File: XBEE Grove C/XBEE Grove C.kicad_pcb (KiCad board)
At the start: 2 copper layers, 53.7 x 72.6 mm, 47 parts, among them J12 TSW-102-07-G-S, J13 TSW-103-07-G-S, J2 B2B-PH-K-S, Q1 SI2323DS-T1-E3, U1 FT232RL-REEL, U2 RT9167A-33GB

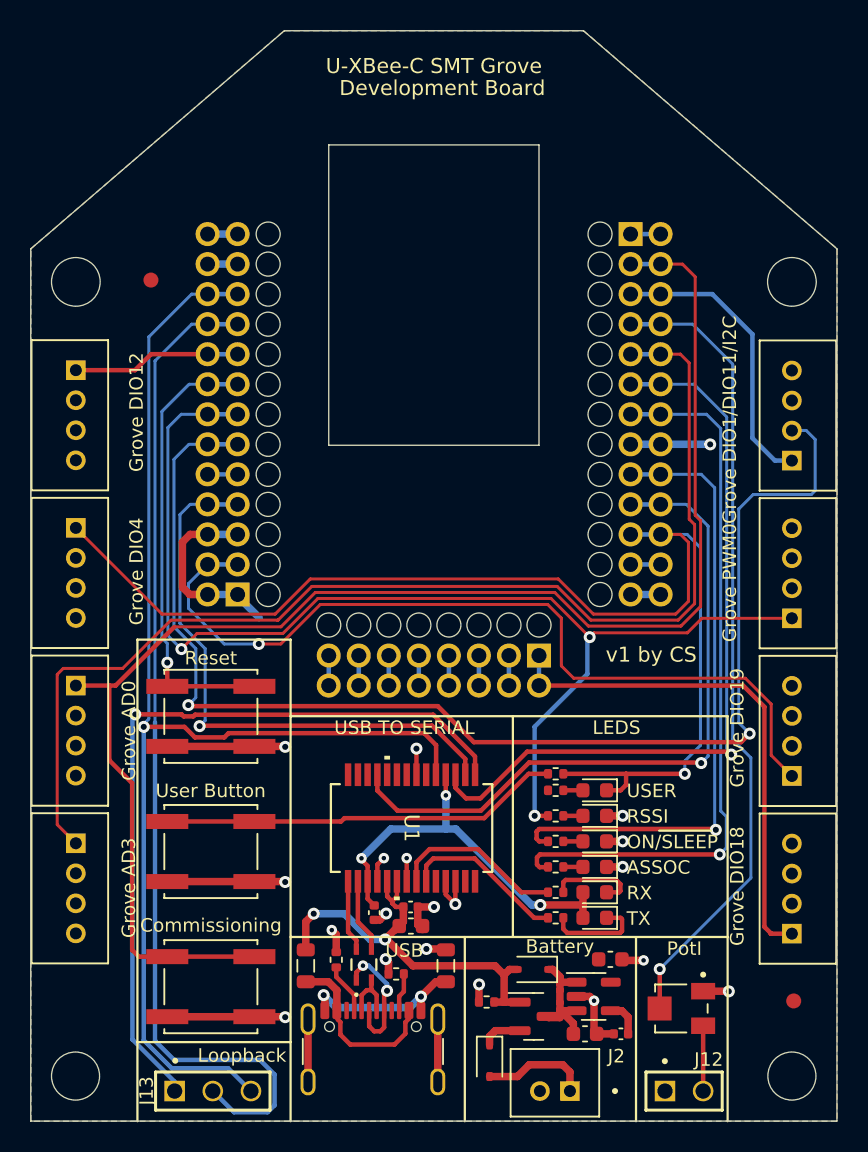
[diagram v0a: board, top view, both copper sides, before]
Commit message: Add files via upload
Corrected L1 and L2 footprints and uploaded boardview file for use with OpenBoardView.
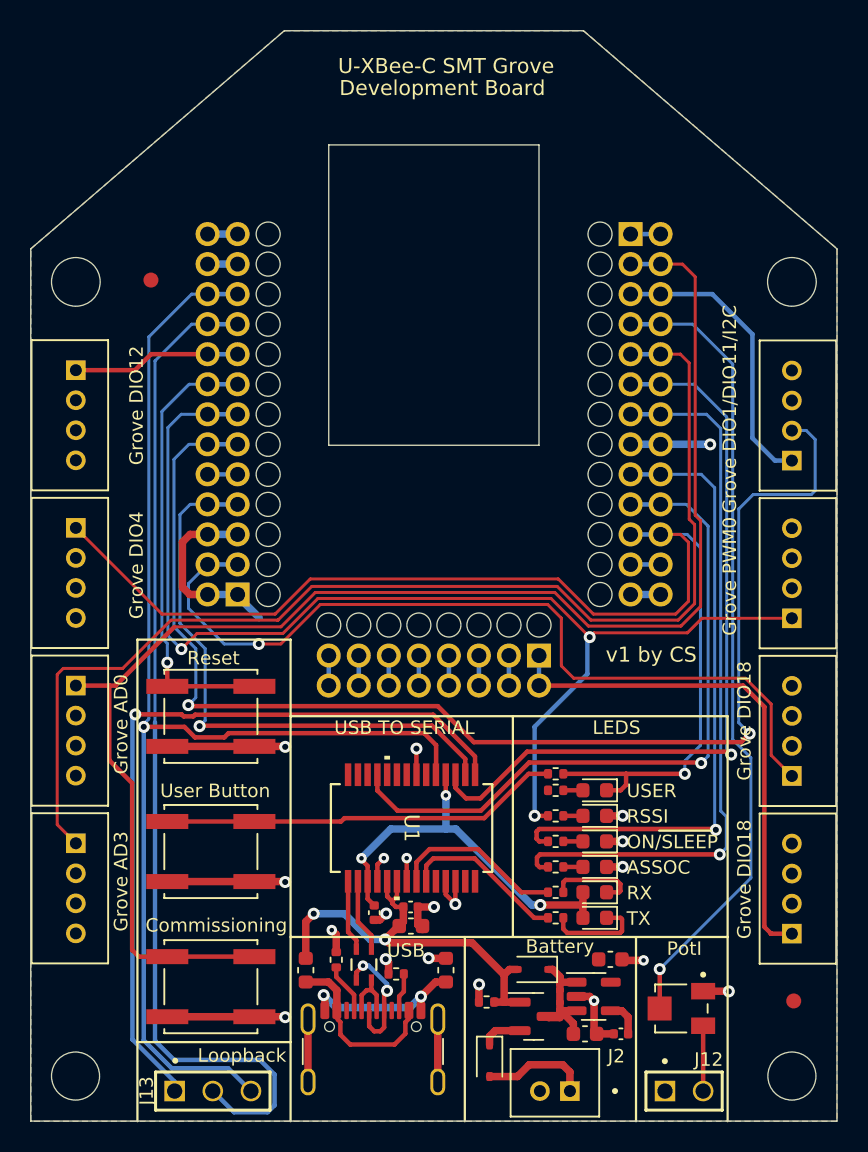
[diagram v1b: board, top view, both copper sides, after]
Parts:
- removed Commissioning, Reset: KSC421J70SHLFS, XBEE_Grove_C:SW_KSC421J70SHLFS
- removed Grove AD0: 110990030, XBEE_Grove_C:SEEED_110990030
- removed Grove AD3: 110990030, XBEE_Grove_C:SEEED_110990030
- removed Grove DIO1/DIO11/I2C: 110990030, XBEE_Grove_C:SEEED_110990030
- removed Grove DIO12: 110990030, XBEE_Grove_C:SEEED_110990030
- removed Grove DIO18: 110990030, XBEE_Grove_C:SEEED_110990030
- removed Grove DIO19: 110990030, XBEE_Grove_C:SEEED_110990030
- removed Grove DIO4: 110990030, XBEE_Grove_C:SEEED_110990030
- removed Grove PWM0: 110990030, XBEE_Grove_C:SEEED_110990030
- removed U-XBee-C SMT Grove: ~, XBEE_Grove_C:XBEE_SMT
- removed USB: USB_C_Receptacle_USB2.0_16P, Connector_USB:USB_C_Receptacle_GCT_USB4105-xx-A_16P_TopMnt_Horizontal
- removed User Button: KSC421J70SHLFS, XBEE_Grove_C:SW_KSC421J70SHLFS
- added J1: ~, XBEE_Grove_C:XBEE_SMT, F.Cu at (146.8, 85.4)
- added J10: 110990030, XBEE_Grove_C:SEEED_110990030, F.Cu at (170.6, 95.7)
- added J11: 110990030, XBEE_Grove_C:SEEED_110990030, F.Cu at (170.6, 106.2)
- added J3: USB_C_Receptacle_USB2.0_16P, Connector_USB:USB_C_Receptacle_GCT_USB4105-xx-A_16P_TopMnt_Horizontal, F.Cu at (142.7, 118.0)
- added J4: 110990030, XBEE_Grove_C:SEEED_110990030, F.Cu at (123.0, 74.7)
- added J5: 110990030, XBEE_Grove_C:SEEED_110990030, F.Cu at (123.0, 85.2)
- added J6: 110990030, XBEE_Grove_C:SEEED_110990030, F.Cu at (123.0, 95.7)
- added J7: 110990030, XBEE_Grove_C:SEEED_110990030, F.Cu at (123.0, 106.2)
- added J8: 110990030, XBEE_Grove_C:SEEED_110990030, F.Cu at (170.6, 74.7)
- added J9: 110990030, XBEE_Grove_C:SEEED_110990030, F.Cu at (170.6, 85.2)
- added S1: KSC421J70SHLFS, XBEE_Grove_C:SW_KSC421J70SHLFS, F.Cu at (131.9, 94.8)
- added S2: KSC421J70SHLFS, XBEE_Grove_C:SW_KSC421J70SHLFS, F.Cu at (131.9, 103.8)
- added S3: KSC421J70SHLFS, XBEE_Grove_C:SW_KSC421J70SHLFS, F.Cu at (131.9, 112.8)
- L1, L2: footprint Inductor_SMD:L_0805_2012Metric -> Inductor_SMD:L_0603_1608Metric
- moved L1 0.29 mm to (138.3, 111.7)
- moved L2 0.29 mm to (147.6, 111.7)
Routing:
- net VBUS: track 28.1 -> 29.0 mm
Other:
- board text added: "Commissioning"
- board text added: "Grove AD0"
- board text added: "Grove AD3"
- board text added: "Grove DIO1/DIO11/I2C"
- board text added: "Grove DIO12"
- board text added: "Grove DIO18"
- board text added: "Grove DIO4"
- board text added: "Grove PWM0"
- board text added: "Reset"
- board text added: "U-XBee-C SMT Grove"
- board text added: "USB"
- board text added: "User Button"

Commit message: Add files via upload
Updated to v2 (all connectors now have the same number scheme as the original).
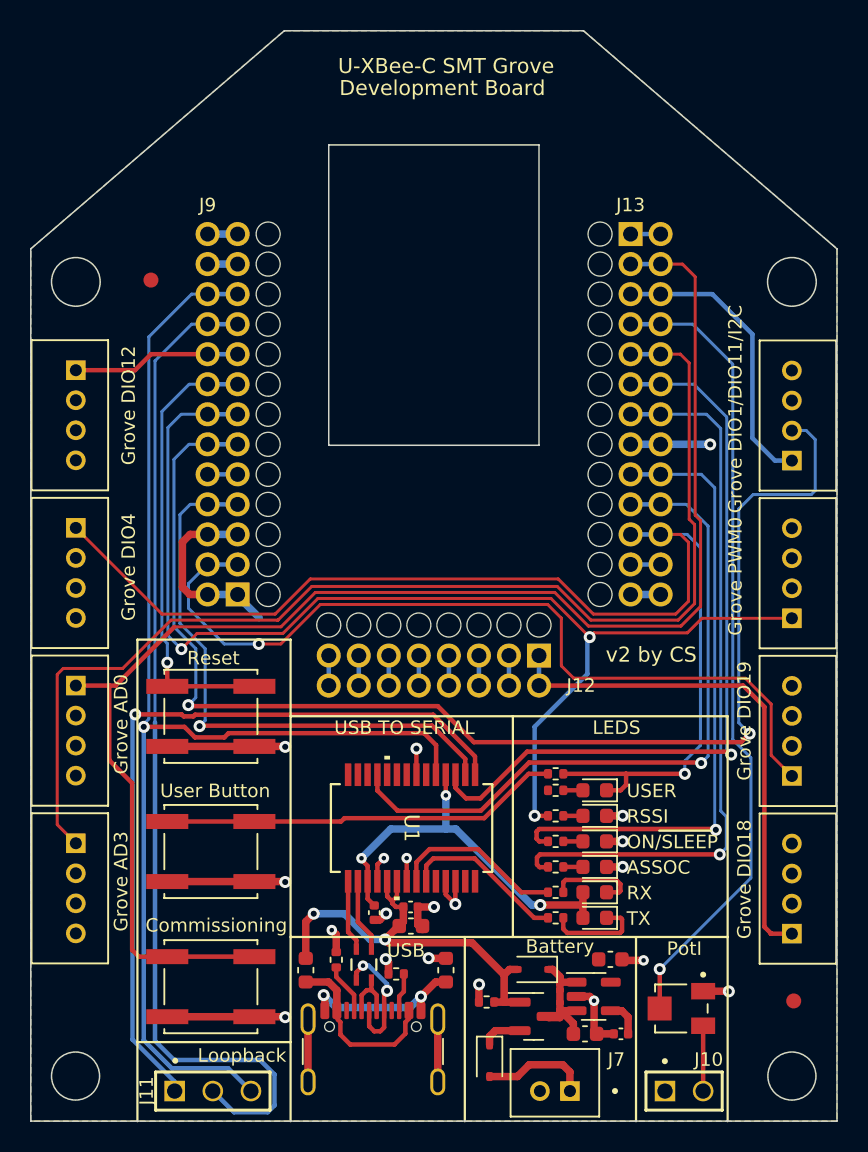
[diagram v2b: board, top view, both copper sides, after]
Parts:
- removed the J1 at (146.8, 85.4)
- added FID1: Fiducial, Fiducial:Fiducial_1mm_Mask2mm, F.Cu at (128.0, 65.7)
- added FID2: Fiducial, Fiducial:Fiducial_1mm_Mask2mm, F.Cu at (170.8, 113.7)
- added J12: ~, XBEE_Grove_C:XBEE_SMT_P14-21, F.Cu at (146.8, 85.4)
- added J13: ~, XBEE_Grove_C:XBEE_SMT_P22-34, F.Cu at (146.8, 85.4)
- added J9: ~, XBEE_Grove_C:XBEE_SMT_P1-13, F.Cu at (146.8, 85.4)
- renumbered J4 to J1, J12 to J10, J13 to J11, J10 to J14, J11 to J15, J5 to J2, J6 to J3, J7 to J4, J8 to J5, J9 to J6, J2 to J7, J3 to J8
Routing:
- net unconnected-(J9-DEBUG/SWDIO_1-Pad9): track 0.00 -> 2.00 mm
- net unconnected-(J13-SWCLK_1-Pad23): track 0.00 -> 2.00 mm
- net unconnected-(J13-RF_SELECT-Pad34): track 0.00 -> 2.00 mm
- net unconnected-(J12-SPI_SSEL/DIO17-Pad20): track 0.00 -> 2.00 mm
- net unconnected-(J12-SPI_MOSI/DIO16-Pad19): track 0.00 -> 2.00 mm
- net unconnected-(J12-SPI_MISO/DIO15-Pad18): track 0.00 -> 2.00 mm
- net unconnected-(J12-JTMS/SWDIO_0-Pad14): track 0.00 -> 2.00 mm
- net unconnected-(J12-JTDO/SWO_0-Pad16): track 0.00 -> 2.00 mm
- net unconnected-(J12-JTDI/SWO_1-Pad15): track 0.00 -> 2.00 mm
- net unconnected-(J12-JTCK/SWCLK_0-Pad17): track 0.00 -> 2.00 mm
- net unconnected-(J1-SWCLK_1-Pad23): track 2.00 -> 0.00 mm
- net unconnected-(J1-SPI_SSEL/DIO17-Pad20): track 2.00 -> 0.00 mm
- net unconnected-(J1-SPI_MOSI/DIO16-Pad19): track 2.00 -> 0.00 mm
- net unconnected-(J1-SPI_MISO/DIO15-Pad18): track 2.00 -> 0.00 mm
- net unconnected-(J1-RF_SELECT-Pad34): track 2.00 -> 0.00 mm
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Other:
- outline, holes or cut-outs redrawn
- board text added: "Grove DIO19"
- board text added: "v2 by CS"
- board text removed: "v1 by CS"

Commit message: Add files via upload
Updated schematic and boardview to match the original part numbers as best I could.
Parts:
- turned R14 to 180 degrees
- renumbered C4 to C10, C1 to C4, C3 to C5, C2 to C6, C6 to C7, C5 to C8, D3 to DS1, D4 to DS2, D5 to DS3, D7 to DS4, D8 to DS5, D6 to DS6, L3 to L2, L2 to L3, R4 to R1, R3 to R10, R5 to R11, R6 to R12, R7 to R13, R9 to R14, R8 to R15, R1 to R2, R2 to R3, R10 to R5, R11 to R6, S3 to S2, S2 to S3
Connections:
- DS6 pad 2: Net-(D6-A) -> Net-(DS6-A)
- R14 pad 1: +3.3V -> Net-(DS6-A)
- R14 pad 2: Net-(D6-A) -> +3.3V
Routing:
- net Net-(DS6-A): track 0.00 -> 1.31 mm
- net Net-(D6-A): track 1.31 -> 0.00 mm

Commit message: Add files via upload
Included 76002056 part number for the SMT connectors.
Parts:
- J12, J13, J9: value ~ -> 76002056
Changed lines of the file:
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@@
 			)
 		)
-		(property "Value" "~"
+		(property "Value" "76002056"
 			(at -13.6 -24.85 0)
 			(unlocked yes)
@@
 			)
 		)
-		(property "Value" "~"
+		(property "Value" "76002056"
 			(at 15.15 -24.9 0)
 			(unlocked yes)
@@
 			)
 		)
-		(property "Value" "~"
+		(property "Value" "76002056"
 			(at 11.825 7.225 0)
 			(unlocked yes)
